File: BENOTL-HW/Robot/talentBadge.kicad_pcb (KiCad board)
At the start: 2 copper layers, 93.8 x 102.7 mm, 64 parts, among them P1 USB_A, P2 OLED, P3 Batt, P4 PS, P5 sd_card_spi, Q1 MMBT3904, Q2 MMBT3904, Q3 IR phototransistor, SW1 B1, SW2 B2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

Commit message: Pre-routeo
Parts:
- added R15: 10K, Resistors_SMD:R_0805_HandSoldering, F.Cu at (75.3, 77.1)
- C1, C2, C3, C4, C5, C6, D2, F1, P1, P3, P4, P5, Q1, Q2, R10, R11, R12, R13, R4, R5, U2, U3, U4: moved to B.Cu
- U1: footprint talentBadge:ESP-12E_SMD -> ESP8266:ESP-12E; moved to B.Cu
- moved R7 153.6 mm to (61.1, 142.7)
- moved C6 149.3 mm to (65.0, 78.3)
- moved R6 148.7 mm to (59.1, 138.4)
- moved R13 147.5 mm to (65.2, 74.2)
- moved C5 145.8 mm to (65.1, 76.2)
- moved R12 145.5 mm to (65.2, 72.1), turned to 180 degrees
- moved C15 144.5 mm to (66.5, 137.2)
- moved R14 140.6 mm to (72.1, 98.6)
- moved R10 140.3 mm to (65.1, 67.9)
- moved R11 136.2 mm to (65.2, 70.0)
- moved SW3 134.5 mm to (36.8, 92.2)
- moved R3 131.7 mm to (75.4, 79.3)
- moved C17 128.9 mm to (57.1, 119.9), turned to 90 degrees
- moved C10 127.4 mm to (69.3, 110.2)
- moved C8 125.3 mm to (65.0, 84.5)
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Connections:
- net Net-(R2-Pad2) renamed /GPIO2
- P2 pad 1: +3V3 -> GND
- P2 pad 2: GND -> +3V3
- U3 pad 3: Net-(P1-Pad3) -> Net-(P1-Pad2)
- U3 pad 4: Net-(P1-Pad2) -> Net-(P1-Pad3)

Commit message: Routeo para revision
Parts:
- R1, R15, R3: moved to B.Cu
- U1: footprint ESP8266:ESP-12E -> RF_Modules:ESP-12E
- moved SW1 64.4 mm to (36.6, 91.4)
- moved R6 46.8 mm to (36.8, 97.3)
- moved R7 30.1 mm to (91.3, 142.7)
- moved R8 29.6 mm to (55.5, 103.9)
- moved R4 26.7 mm to (92.0, 112.3)
- moved SW3 25.7 mm to (55.6, 109.7)
- moved R5 22.1 mm to (97.6, 112.3), turned to 180 degrees
- moved Q2 15.2 mm to (99.8, 115.6)
- moved C1 13.3 mm to (90.4, 130.6), turned to 180 degrees
- moved F1 11.9 mm to (98.0, 128.8), turned to 180 degrees
- moved Q1 8.59 mm to (95.0, 115.6), turned to 180 degrees
- moved U1 7.96 mm to (88.4, 71.1)
- moved C3 7.92 mm to (85.1, 97.0), turned to 180 degrees
- moved C4 5.91 mm to (85.9, 110.5), turned to 180 degrees
- moved D2 5.86 mm to (92.2, 98.8)
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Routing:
- net +3V3: track 0.00 -> 387.3 mm, vias 0 -> 11
- net GND: track 0.00 -> 274.7 mm, vias 0 -> 17
- net RST: track 0.00 -> 120.2 mm, vias 0 -> 3
- net B2: track 0.00 -> 93.8 mm, vias 0 -> 3
- net B1: track 0.00 -> 84.8 mm, vias 0 -> 1
- net TXD: track 0.00 -> 68.2 mm, vias 0 -> 4
- net RXD: track 0.00 -> 62.9 mm, vias 0 -> 2
- net GPIO0: track 0.00 -> 52.3 mm, vias 0 -> 2
- net CS: track 0.00 -> 45.5 mm
- net MISO: track 0.00 -> 44.2 mm
- net IRT: track 0.00 -> 44.0 mm, vias 0 -> 1
- net /VBUS: track 0.00 -> 42.1 mm, vias 0 -> 2
- net MOSI: track 0.00 -> 38.8 mm, vias 0 -> 2
- net IRL: track 0.00 -> 37.8 mm, vias 0 -> 1
- net Net-(C3-Pad1): track 0.00 -> 34.9 mm, vias 0 -> 1
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- added copper zone on B.Cu, net GND
- added copper zone on F.Cu, net GND
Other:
- net class Default: trace_width 0.25 -> 0.3
- net class VCC added: clearance 0.2, trace_width 0.4, via_dia 0.6, via_drill 0.4

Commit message: acomodo de etiquetas
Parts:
- P1: value USB_A -> USB
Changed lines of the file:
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@@
   (general
     (links 155)
-    (no_connects 4)
+    (no_connects 25)
     (area 25.146 49.608325 122.11082 161.364075)
     (thickness 1.6)
@@
     (tags "capacitor 0805")
     (attr smd)
-    (fp_text reference C5 (at 0 1.75) (layer B.SilkS)
+    (fp_text reference C5 (at 3.44 0.204) (layer B.SilkS)
       (effects (font (size 1 1) (thickness 0.15)) (justify mirror))
     )
@@
       (effects (font (size 1 1) (thickness 0.15)) (justify mirror))
     )
-    (fp_text user %R (at 0 1.75) (layer B.Fab)
+    (fp_text user %R (at 3.186 1.982) (layer B.Fab)
       (effects (font (size 1 1) (thickness 0.15)) (justify mirror))
     )
@@
     (tags "capacitor 0805")
     (attr smd)
-    (fp_text reference C6 (at 0 1.75) (layer B.SilkS)
+    (fp_text reference C6 (at 3.286 -0.038) (layer B.SilkS)
       (effects (font (size 1 1) (thickness 0.15)) (justify mirror))
     )
@@
       (effects (font (size 1 1) (thickness 0.15)) (justify mirror))
     )
-    (fp_text user %R (at 0 1.75) (layer B.Fab)
+    (fp_text user %R (at 3.286 -0.038) (layer B.Fab)
       (effects (font (size 1 1) (thickness 0.15)) (justify mirror))
     )
@@
     (tags "capacitor 0805")
     (attr smd)
-    (fp_text reference C7 (at 0 -1.75) (layer F.SilkS)
+    (fp_text reference C7 (at -3.556 0) (layer F.SilkS)
       (effects (font (size 1 1) (thickness 0.15)))
     )
@@
       (effects (font (size 1 1) (thickness 0.15)))
     )
-    (fp_text user %R (at 0 -1.75) (layer F.Fab)
+    (fp_text user %R (at 3.556 0) (layer F.Fab)
       (effects (font (size 1 1) (thickness 0.15)))
     )
@@
     (tags "Diode SMA (DO-214AC)")
     (attr smd)
-    (fp_text reference D2 (at 0 2.5) (layer B.SilkS)
+    (fp_text reference D2 (at -4.604 0.254) (layer B.SilkS)
       (effects (font (size 1 1) (thickness 0.15)) (justify mirror))
     )
@@
       (effects (font (size 1 1) (thickness 0.15)) (justify mirror))
     )
-    (fp_text user %R (at 0 2.5) (layer B.Fab)
+    (fp_text user %R (at -4.604 0.254) (layer B.Fab)
       (effects (font (size 1 1) (thickness 0.15)) (justify mirror))
     )
@@
       (effects (font (size 1 1) (thickness 0.15)) (justify mirror))
     )
-    (fp_text value USB_A (at -1.675 -3.05 270) (layer B.SilkS)
+    (fp_text value USB (at 0.284 4.966 270) (layer B.SilkS)
       (effects (font (size 1 1) (thickness 0.15)) (justify mirror))
     )
@@
     (tags SOT-23)
     (attr smd)
-    (fp_text reference Q1 (at 0 2.5 180) (layer B.SilkS)
+    (fp_text reference Q1 (at 3.286 0 180) (layer B.SilkS)
       (effects (font (size 1 1) (thickness 0.15)) (justify mirror))
     )
@@
     (tags SOT-23)
     (attr smd)
-    (fp_text reference Q2 (at 0 2.5) (layer B.SilkS)
+    (fp_text reference Q2 (at 3.032 0) (layer B.SilkS)
       (effects (font (size 1 1) (thickness 0.15)) (justify mirror))
     )
@@
     (tags "resistor 0805")
     (attr smd)
-    (fp_text reference R3 (at 0 1.7) (layer B.SilkS)
+    (fp_text reference R3 (at -3.488 -0.042) (layer B.SilkS)
       (effects (font (size 1 1) (thickness 0.15)) (justify mirror))
     )
@@
     (tags "resistor 0805")
     (attr smd)
-    (fp_text reference R10 (at 0 1.7) (layer B.SilkS)
+    (fp_text reference R10 (at 3.89 0.254) (layer B.SilkS)
       (effects (font (size 1 1) (thickness 0.15)) (justify mirror))
     )
@@
     (tags "resistor 0805")
     (attr smd)
-    (fp_text reference R11 (at 0 1.7 180) (layer B.SilkS)
+    (fp_text reference R11 (at -3.984 0 180) (layer B.SilkS)
       (effects (font (size 1 1) (thickness 0.15)) (justify mirror))
     )
@@
     (tags "resistor 0805")
     (attr smd)
-    (fp_text reference R12 (at 0 1.7 180) (layer B.SilkS)
+    (fp_text reference R12 (at -3.928 0.198 180) (layer B.SilkS)
       (effects (font (size 1 1) (thickness 0.15)) (justify mirror))
     )
@@
     (tags "resistor 0805")
     (attr smd)
-    (fp_text reference R13 (at 0 1.7 180) (layer B.SilkS)
+    (fp_text reference R13 (at -3.928 -0.008 180) (layer B.SilkS)
       (effects (font (size 1 1) (thickness 0.15)) (justify mirror))
     )
@@
     (tags "CMS SOT")
     (attr smd)
-    (fp_text reference U4 (at 0 4.5 180) (layer B.SilkS)
+    (fp_text reference U4 (at 5.588 0 180) (layer B.SilkS)
       (effects (font (size 1 1) (thickness 0.15)) (justify mirror))
     )
@@
     (tags "resistor 0805")
     (attr smd)
-    (fp_text reference R15 (at 0 1.7) (layer B.SilkS)
-      (effects (font (size 1 1) (thickness 0.15)) (justify mirror))
-    )
+    (fp_text reference R15 (at -3.926 0.106) (layer B.SilkS)
+      (effects (font (size 1 1) (thickness 0.15)) (justify mirror))
+    )

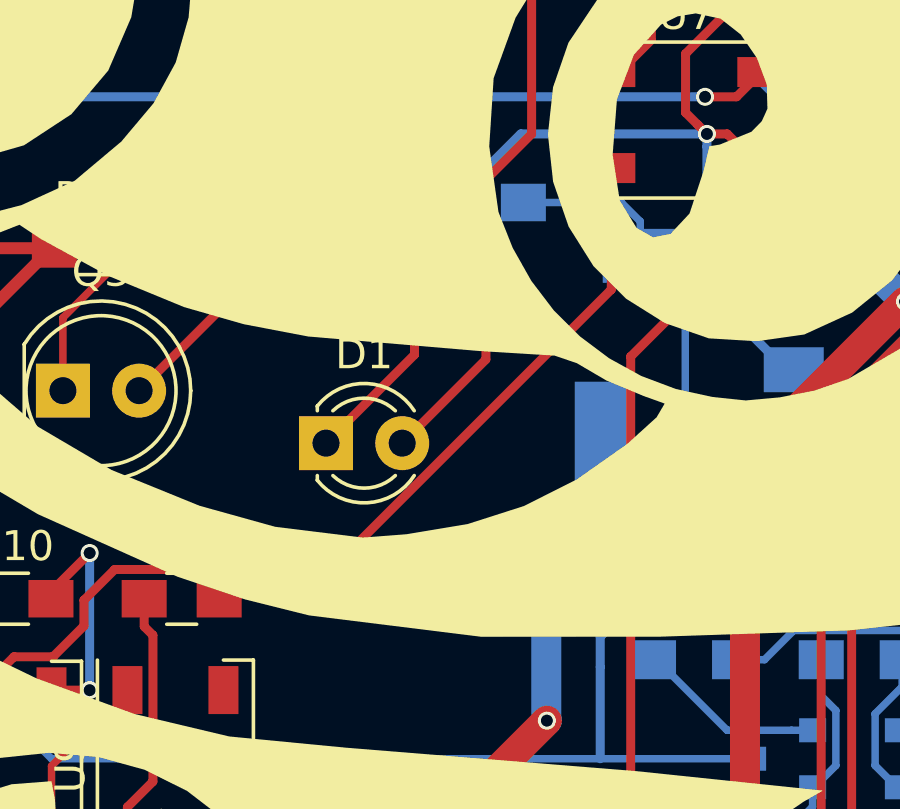
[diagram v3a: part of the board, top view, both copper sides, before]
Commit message: Update C4, C3 y C5
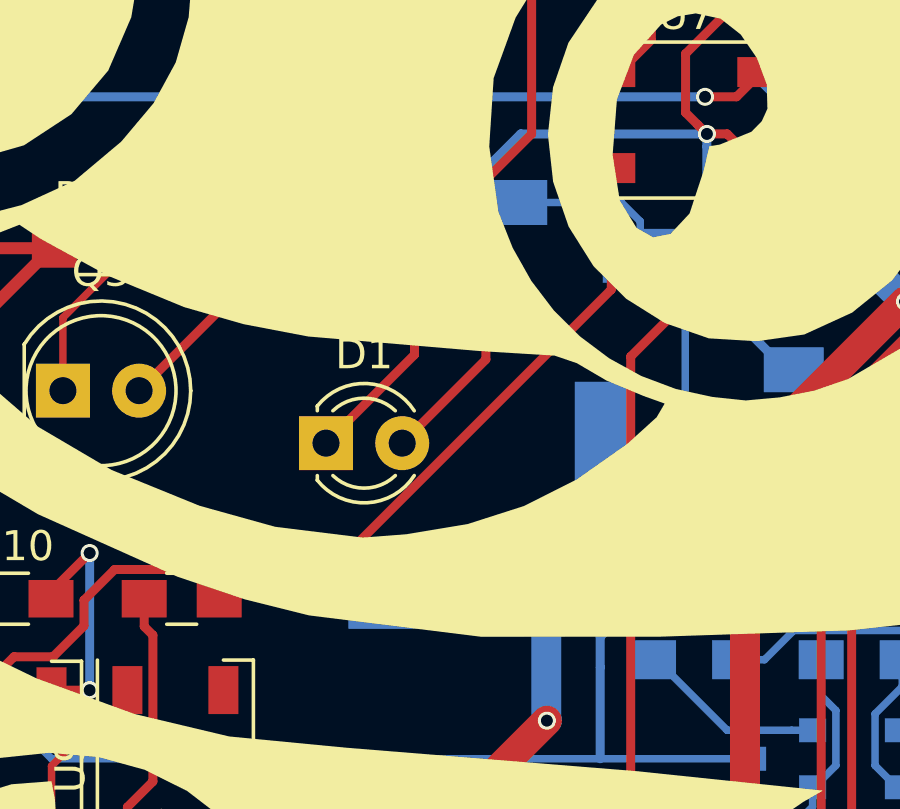
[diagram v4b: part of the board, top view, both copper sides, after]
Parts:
- C3, C4: footprint Capacitors_SMD:C_0805_HandSoldering -> Capacitors_Tantalum_SMD:CP_Tantalum_Case-A_EIA-3216-18_Hand
- P1: value USB -> USB_A
- moved C4 1.75 mm to (84.1, 110.5)
- moved C3 1.56 mm to (83.5, 97.0)
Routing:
- net GND: track 274.7 -> 271.3 mm
- net Net-(C3-Pad1): track 34.9 -> 38.2 mm
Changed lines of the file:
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@@
   (general
     (links 155)
-    (no_connects 25)
-    (area 25.146 49.608325 122.11082 161.364075)
+    (no_connects 4)
+    (area 0 0 0 0)
     (thickness 1.6)
     (drawings 0)
@@
   )
   (module Capacitors_SMD:C_0805_HandSoldering (layer B.Cu)
-    (at 85.09 97.028 180)
-    (descr "Capacitor SMD 0805, hand soldering")
-    (tags "capacitor 0805")
-    (attr smd)
-    (fp_text reference C3 (at 0 1.75 180) (layer B.SilkS)
-      (effects (font (size 1 1) (thickness 0.15)) (justify mirror))
-    )
-    (fp_text value 4.7uF (at 0 -1.75 180) (layer B.Fab)
-      (effects (font (size 1 1) (thickness 0.15)) (justify mirror))
-    )
-    (fp_text user %R (at 0 1.75 180) (layer B.Fab)
-      (effects (font (size 1 1) (thickness 0.15)) (justify mirror))
-    )
-    (fp_line (start -1 -0.62) (end -1 0.62) (layer B.Fab) (width 0.1))
-    (fp_line (start 1 -0.62) (end -1 -0.62) (layer B.Fab) (width 0.1))
-    (fp_line (start 1 0.62) (end 1 -0.62) (layer B.Fab) (width 0.1))
-    (fp_line (start -1 0.62) (end 1 0.62) (layer B.Fab) (width 0.1))
-    (fp_line (start 0.5 0.85) (end -0.5 0.85) (layer B.SilkS) (width 0.12))
-    (fp_line (start -0.5 -0.85) (end 0.5 -0.85) (layer B.SilkS) (width 0.12))
-    (fp_line (start -2.25 0.88) (end 2.25 0.88) (layer B.CrtYd) (width 0.05))
-    (fp_line (start -2.25 0.88) (end -2.25 -0.87) (layer B.CrtYd) (width 0.05))
-    (fp_line (start 2.25 -0.87) (end 2.25 0.88) (layer B.CrtYd) (width 0.05))
-    (fp_line (start 2.25 -0.87) (end -2.25 -0.87) (layer B.CrtYd) (width 0.05))
-    (pad 1 smd rect (at -1.25 0 180) (size 1.5 1.25) (layers B.Cu B.Paste B.Mask)
-      (net 3 "Net-(C3-Pad1)"))
-    (pad 2 smd rect (at 1.25 0 180) (size 1.5 1.25) (layers B.Cu B.Paste B.Mask)
-      (net 2 GND))
-    (model Capacitors_SMD.3dshapes/C_0805.wrl
-      (at (xyz 0 0 0))
-      (scale (xyz 1 1 1))
-      (rotate (xyz 0 0 0))
-    )
-  )
-  (module Capacitors_SMD:C_0805_HandSoldering (layer B.Cu)
-    (at 85.852 110.49 180)
-    (descr "Capacitor SMD 0805, hand soldering")
-    (tags "capacitor 0805")
-    (attr smd)
-    (fp_text reference C4 (at 0 1.75 180) (layer B.SilkS)
-      (effects (font (size 1 1) (thickness 0.15)) (justify mirror))
-    )
-    (fp_text value 4.7uF (at 0 -1.75 180) (layer B.Fab)
-      (effects (font (size 1 1) (thickness 0.15)) (justify mirror))
-    )
-    (fp_text user %R (at 0 1.75 180) (layer B.Fab)
-      (effects (font (size 1 1) (thickness 0.15)) (justify mirror))
-    )
-    (fp_line (start -1 -0.62) (end -1 0.62) (layer B.Fab) (width 0.1))
-    (fp_line (start 1 -0.62) (end -1 -0.62) (layer B.Fab) (width 0.1))
-    (fp_line (start 1 0.62) (end 1 -0.62) (layer B.Fab) (width 0.1))
-    (fp_line (start -1 0.62) (end 1 0.62) (layer B.Fab) (width 0.1))
-    (fp_line (start 0.5 0.85) (end -0.5 0.85) (layer B.SilkS) (width 0.12))
-    (fp_line (start -0.5 -0.85) (end 0.5 -0.85) (layer B.SilkS) (width 0.12))
-    (fp_line (start -2.25 0.88) (end 2.25 0.88) (layer B.CrtYd) (width 0.05))
-    (fp_line (start -2.25 0.88) (end -2.25 -0.87) (layer B.CrtYd) (width 0.05))
-    (fp_line (start 2.25 -0.87) (end 2.25 0.88) (layer B.CrtYd) (width 0.05))
-    (fp_line (start 2.25 -0.87) (end -2.25 -0.87) (layer B.CrtYd) (width 0.05))
-    (pad 1 smd rect (at -1.25 0 180) (size 1.5 1.25) (layers B.Cu B.Paste B.Mask)
-      (net 1 +3V3))
-    (pad 2 smd rect (at 1.25 0 180) (size 1.5 1.25) (layers B.Cu B.Paste B.Mask)
-      (net 2 GND))
-    (model Capacitors_SMD.3dshapes/C_0805.wrl
-      (at (xyz 0 0 0))
-      (scale (xyz 1 1 1))
-      (rotate (xyz 0 0 0))
-    )
-  )
-  (module Capacitors_SMD:C_0805_HandSoldering (layer B.Cu)
     (at 65.14 76.25)
     (descr "Capacitor SMD 0805, hand soldering")
@@
       (effects (font (size 1 1) (thickness 0.15)) (justify mirror))
     )
-    (fp_text value USB (at 0.284 4.966 270) (layer B.SilkS)
+    (fp_text value USB_A (at 0.284 4.966 270) (layer B.SilkS)
       (effects (font (size 1 1) (thickness 0.15)) (justify mirror))
     )
@@
     )
   )
+  (module Capacitors_Tantalum_SMD:CP_Tantalum_Case-A_EIA-3216-18_Hand (layer B.Cu)
+    (at 83.534 97.028 180)
+    (descr "Tantalum capacitor, Case A, EIA 3216-18, 3.2x1.6x1.6mm, Hand soldering footprint")
+    (tags "capacitor tantalum smd")
+    (attr smd)
+    (fp_text reference C3 (at 0 2.55 180) (layer B.SilkS)
+      (effects (font (size 1 1) (thickness 0.15)) (justify mirror))
+    )
+    (fp_text value 4.7uF (at 0 -2.55 180) (layer B.Fab)
+      (effects (font (size 1 1) (thickness 0.15)) (justify mirror))
+    )
+    (fp_text user %R (at 0 0 180) (layer B.Fab)
+      (effects (font (size 0.7 0.7) (thickness 0.105)) (justify mirror))
+    )
+    (fp_line (start -4 1.2) (end -4 -1.2) (layer B.CrtYd) (width 0.05))
+    (fp_line (start -4 -1.2) (end 4 -1.2) (layer B.CrtYd) (width 0.05))
+    (fp_line (start 4 -1.2) (end 4 1.2) (layer B.CrtYd) (width 0.05))
+    (fp_line (start 4 1.2) (end -4 1.2) (layer B.CrtYd) (width 0.05))
+    (fp_line (start -1.6 0.8) (end -1.6 -0.8) (layer B.Fab) (width 0.1))
+    (fp_line (start -1.6 -0.8) (end 1.6 -0.8) (layer B.Fab) (width 0.1))
+    (fp_line (start 1.6 -0.8) (end 1.6 0.8) (layer B.Fab) (width 0.1))
+    (fp_line (start 1.6 0.8) (end -1.6 0.8) (layer B.Fab) (width 0.1))
+    (fp_line (start -1.28 0.8) (end -1.28 -0.8) (layer B.Fab) (width 0.1))
+    (fp_line (start -1.12 0.8) (end -1.12 -0.8) (layer B.Fab) (width 0.1))
+    (fp_line (start -3.9 1.05) (end 1.6 1.05) (layer B.SilkS) (width 0.12))
+    (fp_line (start -3.9 -1.05) (end 1.6 -1.05) (layer B.SilkS) (width 0.12))
+    (fp_line (start -3.9 1.05) (end -3.9 -1.05) (layer B.SilkS) (width 0.12))
+    (pad 1 smd rect (at -2 0 180) (size 3.2 1.5) (layers B.Cu B.Paste B.Mask)
+      (net 3 "Net-(C3-Pad1)"))
+    (pad 2 smd rect (at 2 0 180) (size 3.2 1.5) (layers B.Cu B.Paste B.Mask)
+      (net 2 GND))
+    (model Capacitors_Tantalum_SMD.3dshapes/CP_Tantalum_Case-A_EIA-3216-18.wrl
+      (at (xyz 0 0 0))
+      (scale (xyz 1 1 1))
+      (rotate (xyz 0 0 0))
+    )
+  )
+  (module Capacitors_Tantalum_SMD:CP_Tantalum_Case-A_EIA-3216-18_Hand (layer B.Cu)
+    (at 84.106 110.49 180)
+    (descr "Tantalum capacitor, Case A, EIA 3216-18, 3.2x1.6x1.6mm, Hand soldering footprint")
+    (tags "capacitor tantalum smd")
+    (attr smd)
+    (fp_text reference C4 (at 0 2.55 180) (layer B.SilkS)
+      (effects (font (size 1 1) (thickness 0.15)) (justify mirror))
+    )
+    (fp_text value 4.7uF (at 0 -2.55 180) (layer B.Fab)
+      (effects (font (size 1 1) (thickness 0.15)) (justify mirror))
+    )
+    (fp_text user %R (at 0 0 180) (layer B.Fab)
+      (effects (font (size 0.7 0.7) (thickness 0.105)) (justify mirror))
+    )
+    (fp_line (start -4 1.2) (end -4 -1.2) (layer B.CrtYd) (width 0.05))
+    (fp_line (start -4 -1.2) (end 4 -1.2) (layer B.CrtYd) (width 0.05))
+    (fp_line (start 4 -1.2) (end 4 1.2) (layer B.CrtYd) (width 0.05))
+    (fp_line (start 4 1.2) (end -4 1.2) (layer B.CrtYd) (width 0.05))
+    (fp_line (start -1.6 0.8) (end -1.6 -0.8) (layer B.Fab) (width 0.1))
+    (fp_line (start -1.6 -0.8) (end 1.6 -0.8) (layer B.Fab) (width 0.1))
+    (fp_line (start 1.6 -0.8) (end 1.6 0.8) (layer B.Fab) (width 0.1))
+    (fp_line (start 1.6 0.8) (end -1.6 0.8) (layer B.Fab) (width 0.1))
+    (fp_line (start -1.28 0.8) (end -1.28 -0.8) (layer B.Fab) (width 0.1))
+    (fp_line (start -1.12 0.8) (end -1.12 -0.8) (layer B.Fab) (width 0.1))
+    (fp_line (start -3.9 1.05) (end 1.6 1.05) (layer B.SilkS) (width 0.12))
+    (fp_line (start -3.9 -1.05) (end 1.6 -1.05) (layer B.SilkS) (width 0.12))
+    (fp_line (start -3.9 1.05) (end -3.9 -1.05) (layer B.SilkS) (width 0.12))
+    (pad 1 smd rect (at -2 0 180) (size 3.2 1.5) (layers B.Cu B.Paste B.Mask)
+      (net 1 +3V3))
+    (pad 2 smd rect (at 2 0 180) (size 3.2 1.5) (layers B.Cu B.Paste B.Mask)
+      (net 2 GND))
+    (model Capacitors_Tantalum_SMD.3dshapes/CP_Tantalum_Case-A_EIA-3216-18.wrl
+      (at (xyz 0 0 0))
+      (scale (xyz 1 1 1))
+      (rotate (xyz 0 0 0))
+    )
+  )
   (segment (start 71.882 77.216) (end 73.844 77.216) (width 0.4) (layer B.Cu) (net 1))
   (segment (start 73.844 77.216) (end 73.95 77.11) (width 0.4) (layer B.Cu) (net 1))
@@
   (segment (start 92.456 94.742) (end 93.132 94.742) (width 0.3) (layer F.Cu) (net 2))
   (segment (start 93.132 94.742) (end 94.27 95.88) (width 0.3) (layer F.Cu) (net 2))
-  (segment (start 83.84 97.028) (end 83.965 97.028) (width 0.3) (layer B.Cu) (net 2))
-  (segment (start 83.965 97.028) (end 86.251 94.742) (width 0.3) (layer B.Cu) (net 2))
   (segment (start 86.251 94.742) (end 92.456 94.742) (width 0.3) (layer B.Cu) (net 2))
   (via (at 92.456 94.742) (size 0.6) (drill 0.4) (layers F.Cu B.Cu) (net 2))
@@
   (segment (start 104.57 83.9) (end 105.72 83.9) (width 0.3) (layer F.Cu) (net 2))
   (segment (start 89.154 130.556) (end 89.154 127.508) (width 0.3) (layer B.Cu) (net 2))
+  (segment (start 83.84 97.028) (end 83.965 97.028) (width 0.3) (layer B.Cu) (net 3))
+  (segment (start 83.965 97.028) (end 86.251 94.742) (width 0.3) (layer B.Cu) (net 3))
+  (segment (start 86.34 97.028) (end 89.606 97.028) (width 0.25) (layer B.Cu) (net 3))
+  (segment (start 89.606 97.028) (end 90.234 97.656) (width 0.25) (layer B.Cu) (net 3))
   (segment (start 100.33 106.68) (end 103.886 106.68) (width 0.3) (layer F.Cu) (net 3))
   (segment (start 95.352 107.202) (end 99.808 107.202) (width 0.3) (layer B.Cu) (net 3))
@@
   (segment (start 91.734 103.834) (end 95.102 107.202) (width 0.25) (layer B.Cu) (net 3))
   (segment (start 95.102 107.202) (end 95.352 107.202) (width 0.25) (layer B.Cu) (net 3))
-  (segment (start 86.34 97.028) (end 89.606 97.028) (width 0.25) (layer B.Cu) (net 3))
-  (segment (start 89.606 97.028) (end 90.234 97.656) (width 0.25) (layer B.Cu) (net 3))
   (segment (start 90.234 97.656) (end 90.234 98.806) (width 0.25) (layer B.Cu) (net 3))
   (segment (start 95.366 107.188) (end 95.352 107.202) (width 0.25) (layer B.Cu) (net 3))
